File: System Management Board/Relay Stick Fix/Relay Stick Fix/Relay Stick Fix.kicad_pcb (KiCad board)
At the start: 4 copper layers, 28.2 x 27 mm, 17 parts, among them J1 Conn_02x04, Q1 NMOS

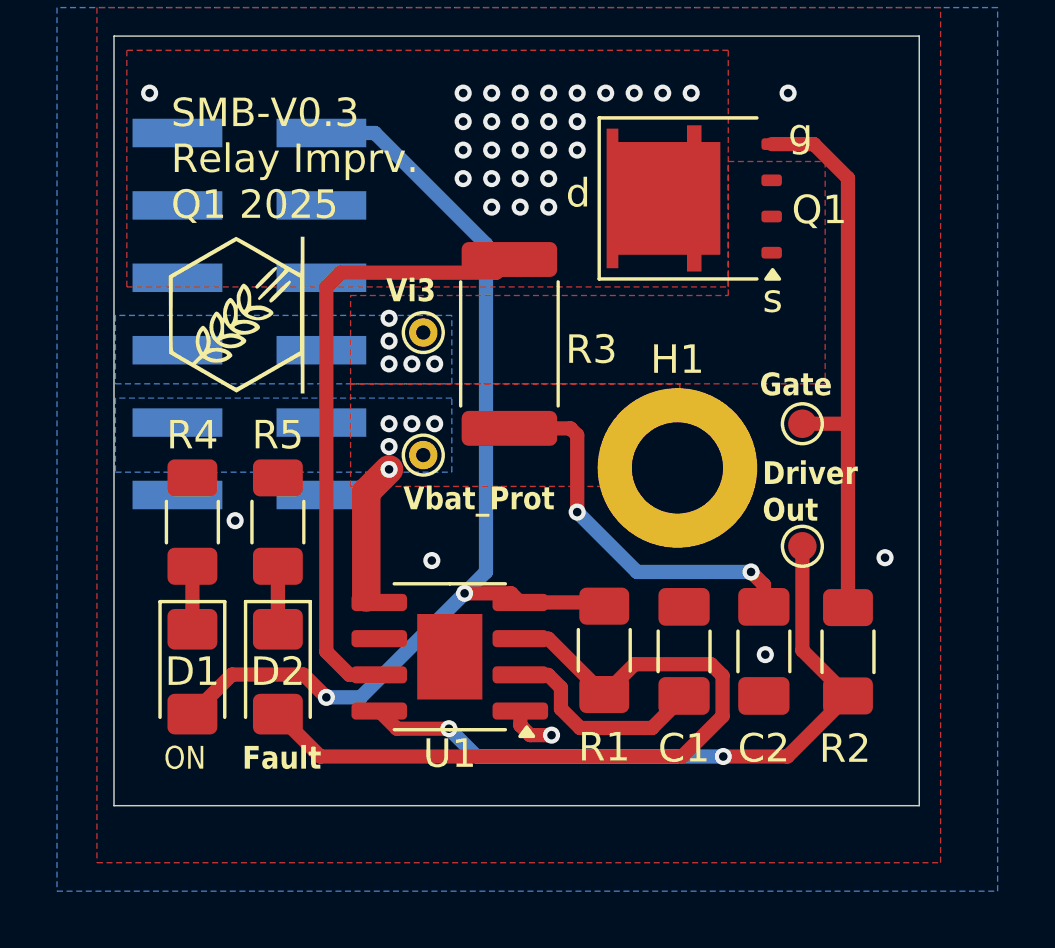
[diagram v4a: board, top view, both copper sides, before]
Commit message: capacitor footprint correction 1210
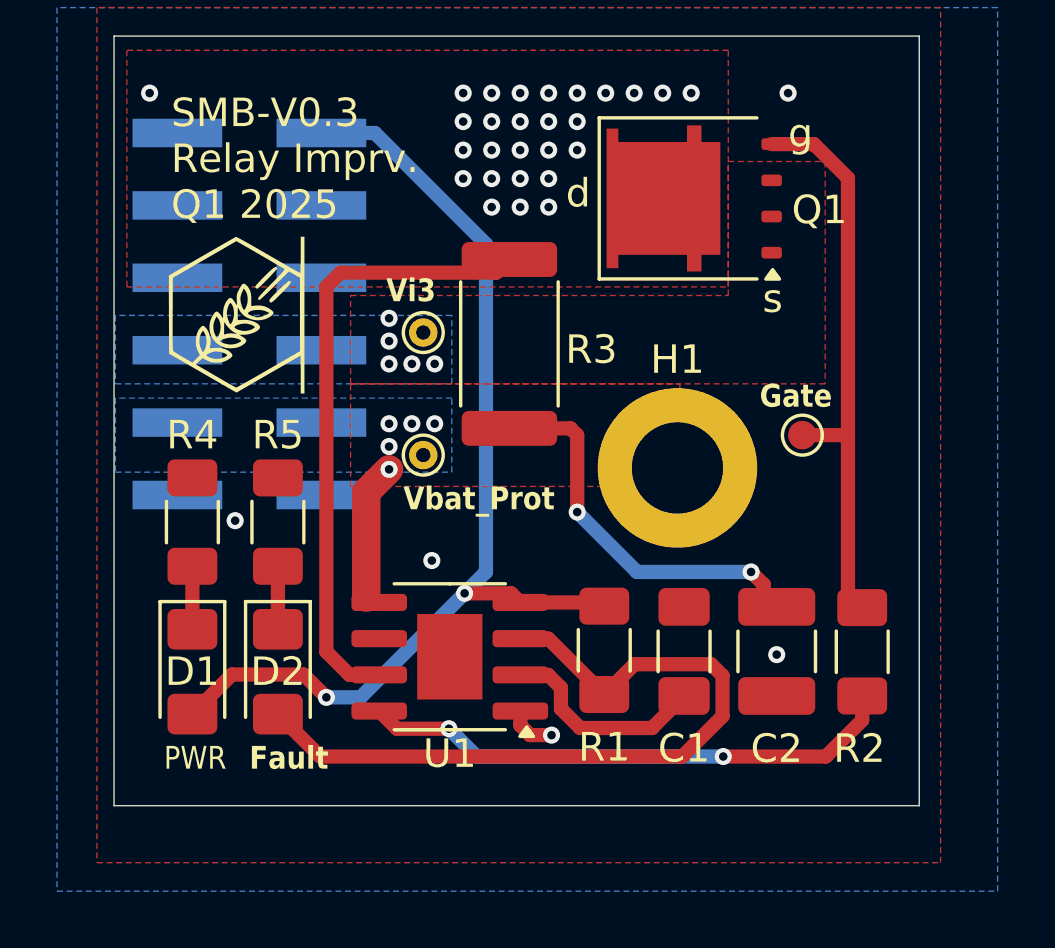
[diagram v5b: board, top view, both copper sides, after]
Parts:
- removed TP1: TestPoint, TestPoint:TestPoint_Pad_D1.0mm
- C2: footprint Capacitor_SMD:C_1206_3216Metric_Pad1.33x1.80mm_HandSolder -> Capacitor_SMD:C_1210_3225Metric_Pad1.33x2.70mm_HandSolder
- J1: value Conn_02x04 -> Conn_02x06
- R4, R5: value 220 -> 280
- moved R2 0.50 mm to (228.0, 138.6)
- moved C2 0.45 mm to (225.0, 138.6)
- moved TP2 0.40 mm to (225.9, 131.0)
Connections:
- net Net-(U1-GATE) renamed /Driver Out
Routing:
- net /Driver Out: track 23.5 -> 19.0 mm
- net GND: vias 7 -> 6
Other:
- board text added: "PWR"
- board text removed: "Driver Out"
- board text removed: "ON"
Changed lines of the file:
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@@
 	(net 6 "/Sense")
 	(net 7 "/Fault")
-	(net 8 "Net-(U1-GATE)")
+	(net 8 "/Driver Out")
 	(net 9 "unconnected-(J1-Pin_3-Pad3)")
 	(net 10 "unconnected-(J1-Pin_4-Pad4)")
@@
 			)
 		)
-		(property "Value" "220"
+		(property "Value" "280"
 			(at 0 1.82 -90)
 			(layer "F.Fab")
@@
 			(layers "F.Cu" "F.Paste" "F.Mask")
 			(roundrect_rratio 0.25)
-			(net 8 "Net-(U1-GATE)")
+			(net 8 "/Driver Out")
 			(pinfunction "GATE")
 			(pintype "input")
@@
 			)
 		)
-		(property "Value" "220"
+		(property "Value" "280"
 			(at 0 1.82 -90)
 			(layer "F.Fab")
@@
 	(footprint "Resistor_SMD:R_1206_3216Metric_Pad1.30x1.75mm_HandSolder"
 		(layer "F.Cu")
-		(at 227.5 138.6 90)
+		(at 228 138.6 90)
 		(descr "Resistor SMD 1206 (3216 Metric), square (rectangular) end terminal, IPC_7351 nominal with elongated pad for handsoldering. (Body size source: IPC-SM-782 page 72, https://www.pcb-3d.com/wordpress/wp-content/uploads/ipc-sm-782a_amendment_1_and_2.pdf), generated with kicad-footprint-generator")
 		(tags "resistor handsolder")
@@
 			(layers "F.Cu" "F.Paste" "F.Mask")
 			(roundrect_rratio 0.192308)
-			(net 8 "Net-(U1-GATE)")
+			(net 8 "/Driver Out")
 			(pintype "passive")
 		)
@@
 		)
 	)
-	(footprint "Capacitor_SMD:C_1206_3216Metric_Pad1.33x1.80mm_HandSolder"
+	(footprint "Capacitor_SMD:C_1210_3225Metric_Pad1.33x2.70mm_HandSolder"
 		(layer "F.Cu")
-		(at 224.55 138.5875 -90)
-		(descr "Capacitor SMD 1206 (3216 Metric), square (rectangular) end terminal, IPC_7351 nominal with elongated pad for handsoldering. (Body size source: IPC-SM-782 page 76, https://www.pcb-3d.com/wordpress/wp-content/uploads/ipc-sm-782a_amendment_1_and_2.pdf), generated with kicad-footprint-generator")
+		(at 225 138.5875 -90)
+		(descr "Capacitor SMD 1210 (3225 Metric), square (rectangular) end terminal, IPC_7351 nominal with elongated pad for handsoldering. (Body size source: IPC-SM-782 page 76, https://www.pcb-3d.com/wordpress/wp-content/uploads/ipc-sm-782a_amendment_1_and_2.pdf), generated with kicad-footprint-generator")
 		(tags "capacitor handsolder")
 		(property "Reference" "C2"
-			(at 3.4 0 180)
+			(at 3.4125 0 0)
 			(layer "F.SilkS")
 			(effects
@@
 		)
 		(property "Value" "10uF"
-			(at 0 1.85 90)
+			(at 0 2.3 -90)
 			(layer "F.Fab")
 			(effects
@@
 			)
 		)
-		(property "Footprint" "Capacitor_SMD:C_1206_3216Metric_Pad1.33x1.80mm_HandSolder"
+		(property "Footprint" "Capacitor_SMD:C_1210_3225Metric_Pad1.33x2.70mm_HandSolder"
 			(at 0 0 -90)
 			(unlocked yes)
@@
 		(attr smd)
 		(fp_line
-			(start -0.711252 0.91)
-			(end 0.711252 0.91)
+			(start -0.711252 1.36)
+			(end 0.711252 1.36)
 			(stroke
 				(width 0.12)
@@
 		)
 		(fp_line
-			(start -0.711252 -0.91)
-			(end 0.711252 -0.91)
+			(start -0.711252 -1.36)
+			(end 0.711252 -1.36)
 			(stroke
 				(width 0.12)
@@
 		)
 		(fp_line
-			(start -2.48 1.15)
-			(end -2.48 -1.15)
+			(start -2.48 1.6)
+			(end -2.48 -1.6)
 			(stroke
 				(width 0.05)
@@
 		)
 		(fp_line
-			(start 2.48 1.15)
-			(end -2.48 1.15)
+			(start 2.48 1.6)
+			(end -2.48 1.6)
 			(stroke
 				(width 0.05)
@@
 		)
 		(fp_line
-			(start -2.48 -1.15)
-			(end 2.48 -1.15)
+			(start -2.48 -1.6)
+			(end 2.48 -1.6)
 			(stroke
 				(width 0.05)
@@
 		)
 		(fp_line
-			(start 2.48 -1.15)
-			(end 2.48 1.15)
+			(start 2.48 -1.6)
+			(end 2.48 1.6)
 			(stroke
 				(width 0.05)
@@
 		)
 		(fp_line
-			(start -1.6 0.8)
-			(end -1.6 -0.8)
+			(start -1.6 1.25)
+			(end -1.6 -1.25)
 			(stroke
 				(width 0.1)
@@
 		)
 		(fp_line
-			(start 1.6 0.8)
-			(end -1.6 0.8)
+			(start 1.6 1.25)
+			(end -1.6 1.25)
 			(stroke
 				(width 0.1)
@@
 		)
 		(fp_line
-			(start -1.6 -0.8)
-			(end 1.6 -0.8)
+			(start -1.6 -1.25)
+			(end 1.6 -1.25)
 			(stroke
 				(width 0.1)
@@
 		)
 		(fp_line
-			(start 1.6 -0.8)
-			(end 1.6 0.8)
+			(start 1.6 -1.25)
+			(end 1.6 1.25)
 			(stroke
 				(width 0.1)
@@
 		)
 		(fp_text user "${REFERENCE}"
-			(at 0 0 90)
+			(at 0 0 -90)
 			(layer "F.Fab")
 			(effects
@@
 		(pad "1" smd roundrect
 			(at -1.5625 0 270)
-			(size 1.325 1.8)
+			(size 1.325 2.7)
 			(layers "F.Cu" "F.Paste" "F.Mask")
 			(roundrect_rratio 0.188679)
@@
 		(pad "2" smd roundrect
 			(at 1.5625 0 270)
-			(size 1.325 1.8)
+			(size 1.325 2.7)
 			(layers "F.Cu" "F.Paste" "F.Mask")
 			(roundrect_rratio 0.188679)
@@
 			(zone_connect 2)
 		)
-		(model "${KICAD8_3DMODEL_DIR}/Capacitor_SMD.3dshapes/C_1206_3216Metric.wrl"
+		(model "${KICAD8_3DMODEL_DIR}/Capacitor_SMD.3dshapes/C_1210_3225Metric.wrl"
 			(offset
 				(xyz 0 0 0)
@@
 	(footprint "TestPoint:TestPoint_Pad_D1.0mm"
 		(layer "F.Cu")
-		(at 225.9 130.6)
+		(at 225.9 131)
 		(descr "SMD pad as test Point, diameter 1.0mm")
 		(tags "test point SMD pad")
@@
 		)
 	)
-	(footprint "TestPoint:TestPoint_Pad_D1.0mm"
-		(layer "F.Cu")
-		(at 225.9 134.9)
-		(descr "SMD pad as test Point, diameter 1.0mm")
-		(tags "test point SMD pad")
-		(property "Reference" "TP1"
-			(at 0 -1.448 0)
-			(layer "F.SilkS")
-			(hide yes)
-			(effects
-				(font
-					(size 1 1)
-					(thickness 0.15)
-				)
-			)
-		)
-		(property "Value" "TestPoint"
-			(at 0 1.55 0)
-			(layer "F.Fab")
-			(effects
-				(font
-					(size 1 1)
-					(thickness 0.15)
-				)
-			)
-		)
-		(property "Footprint" "TestPoint:TestPoint_Pad_D1.0mm"
-			(at 0 0 0)
-			(unlocked yes)
-			(layer "F.Fab")
-			(hide yes)
-			(effects
-				(font
-					(size 1.27 1.27)
-				)
-			)
-		)
-		(property "Datasheet" ""
-			(at 0 0 0)
-			(unlocked yes)
-			(layer "F.Fab")
-			(hide yes)
-			(effects
-				(font
-					(size 1.27 1.27)
-				)
-			)
-		)
-		(property "Description" "test point"
-			(at 0 0 0)
-			(unlocked yes)
-			(layer "F.Fab")
-			(hide yes)
-			(effects
-				(font
-					(size 1.27 1.27)
-				)
-			)
-		)
-		(property ki_fp_filters "Pin* Test*")
-		(sheetname "Root")
-		(sheetfile "Relay Stick Fix.kicad_sch")
-		(attr exclude_from_pos_files)
-		(fp_circle
-			(center 0 0)
-			(end 0 0.7)
-			(stroke
-				(width 0.12)
-				(type solid)
-			)
-			(fill none)
-			(layer "F.SilkS")
-		)
-		(fp_circle
-			(center 0 0)
-			(end 1 0)
-			(stroke
-				(width 0.05)
-				(type solid)
-			)
-			(fill none)
-			(layer "F.CrtYd")
-		)
-		(fp_text user "${REFERENCE}"
-			(at 0 -1.45 0)
-			(layer "F.Fab")
-			(effects
-				(font
-					(size 1 1)
-					(thickness 0.15)
-				)
-			)
-		)
-		(pad "1" smd circle
-			(at 0 0)
-			(size 1 1)
-			(layers "F.Cu" "F.Mask")
-			(net 8 "Net-(U1-GATE)")
-			(pinfunction "1")
-			(pintype "passive")
-		)
-	)
 	(footprint "Connector_PinHeader_2.54mm:PinHeader_2x06_P2.54mm_Vertical_SMD"
 		(layer "B.Cu")
@@
 			)
 		)
-		(property "Value" "Conn_02x04"
+		(property "Value" "Conn_02x06"
 			(at 0 -8.68 180)
 			(layer "B.Fab")
@@
 	)
 	(gr_text "Gate"
-		(at 224.4 129.7 0)
+		(at 224.4 130.1 0)
 		(layer "F.SilkS")
 		(effects
@@
 	)
 	(gr_text "Fault"
-		(at 206.25 142.8 0)
+		(at 206.5 142.8 0)
 		(layer "F.SilkS")
 		(effects
@@
 		)
 	)
-	(gr_text "ON"
+	(gr_text "PWR\n"
 		(at 203.5 142.8 0)
 		(layer "F.SilkS")
@@
 		)
 	)
-	(gr_text "Driver\nOut\n"
-		(at 224.5 134.1 0)
-		(layer "F.SilkS")
-		(effects
-			(font
-				(size 0.8 0.7)
-				(thickness 0.1)
-				(bold yes)
-			)
-			(justify left bottom)
-		)
-	)
 	(gr_text "Vbat_Prot"
 		(at 211.9 133.7 0)
@@
 	)
 	(via
-		(at 228.8 135.3)
-		(size 0.6)
-		(drill 0.3)
-		(layers "F.Cu" "B.Cu")
-		(free yes)
-		(net 1)
-	)
-	(via
 		(at 203 119)
 		(size 0.6)
@@
 	)
 	(via
-		(at 224.6 138.7)
+		(at 225 138.7)
 		(size 0.6)
 		(drill 0.3)
@@
 	)
 	(segment
-		(start 225.375 142.275)
-		(end 227.5 140.15)
-		(width 0.5)
-		(layer "F.Cu")
-		(net 8)
-	)
-	(segment
 		(start 223.125 142.275)
-		(end 225.375 142.275)
+		(end 226.725 142.275)
 		(width 0.5)
 		(layer "F.Cu")
@@
 	)
 	(segment
-		(start 225.9 138.55)
-		(end 225.9 135.3)
+		(start 228 141)
+		(end 228 140.15)
 		(width 0.5)
 		(layer "F.Cu")
@@
 	)
 	(segment
-		(start 227.5 140.15)
-		(end 225.9 138.55)
+		(start 226.725 142.275)
+		(end 228 141)
 		(width 0.5)
 		(layer "F.Cu")
@@
 	)
 	(segment
-		(start 227.5 130.6)
-		(end 225.9 130.6)
+		(start 228 137.05)
+		(end 227.5 136.55)
 		(width 0.5)
 		(layer "F.Cu")
@@
 	)
 	(segment
-		(start 227.5 121.98375)
-		(end 226.30625 120.79)
+		(start 227.5 131)
+		(end 227.5 121.98375)
 		(width 0.5)
 		(layer "F.Cu")
@@
 	)
 	(segment
-		(start 227.5 130.6)
-		(end 227.5 121.98375)
+		(start 227.5 136.55)
+		(end 227.5 131)
 		(width 0.5)
 		(layer "F.Cu")
@@
 	)
 	(segment
-		(start 227.5 137.05)
-		(end 227.5 130.6)
+		(start 226.30625 120.79)
+		(end 224.8225 120.79)
 		(width 0.5)
 		(layer "F.Cu")
@@
 	)
 	(segment
-		(start 226.30625 120.79)
-		(end 224.8225 120.79)
+		(start 227.5 131)
+		(end 225.9 131)
+		(width 0.5)
+		(layer "F.Cu")
+		(net 18)
+	)
+	(segment
+		(start 227.5 121.98375)
+		(end 226.30625 120.79)
 		(width 0.5)
 		(layer "F.Cu")
@@
 	)
 	(group ""
+		(members "bb8eceb2-75df-49de-95a5-31afb5ff107b" "f998aebb-df1a-4666-9337-fedac85aca8c")
+	)
+	(group ""
+		(members "7aa18af9-3efa-4036-90f6-d272eb30f3e6")
+	)
+	(group ""

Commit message: implementing mark's notes
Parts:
- added U2: 74LVC1G04, Package_TO_SOT_SMD:SOT-23-5, F.Cu at (19.9, 37.5)
- C1: value 100nF -> 0.1uF
- R4, R5: value 280 -> 1k
- moved D1 214.7 mm to (18.4, 32.3)
- moved D2 214.7 mm to (21.4, 32.3)
- moved R4 214.7 mm to (18.4, 27.0)
- moved R5 214.7 mm to (21.4, 27.0)
- moved C1 212.0 mm to (35.9, 36.6)
- moved C2 212.0 mm to (39.1, 36.6)
- moved H1 212.0 mm to (35.6, 30.2)
- moved J1 212.0 mm to (20.6, 24.8)
- moved R2 212.0 mm to (42.1, 36.6)
- moved R3 212.0 mm to (29.7, 25.8)
- moved TP2 212.0 mm to (40.0, 29.0)
- moved TP3 212.0 mm to (26.7, 29.7)
- moved TP4 212.0 mm to (26.7, 25.4)
- moved U1 212.0 mm to (27.6, 36.8)
- moved Q1 212.0 mm to (36.2, 20.7)
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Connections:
- D2 pad 2: /Fault -> Net-(D2-A)
- R2 pad 1: /Driver Out -> Net-(U1-GATE)
- U1 pad 5: /Vbat Prot -> Net-(U1-GATE)
- U1 pad 6: unconnected-(U1-NC-Pad6) -> /Sense
- U1 pad 7: /Sense -> unconnected-(U1-NC-Pad7)
- U1 pad 8: /Driver Out -> /Vbat Prot
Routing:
- net Net-(U1-GATE): track 0.00 -> 20.5 mm, vias 0 -> 2
- net /Driver Out: track 19.0 -> 0.00 mm, vias 2 -> 0
- net GND: track 1.74 -> 10.3 mm, vias 6 -> 7
- net /Vbat Prot: track 18.7 -> 24.6 mm, vias 7 -> 9
- net Net-(D2-A): track 0.00 -> 2.80 mm
- net /Fault: track 26.7 -> 29.0 mm
- net /Sense: track 21.8 -> 20.3 mm
- net /5V Bootstrap: track 37.6 -> 38.3 mm

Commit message: zone fix
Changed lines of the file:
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@@
 		(net 1)
 		(net_name "GND")
-		(layers "F.Cu" "In1.Cu")
-		(hatch edge 0.5)
-		(priority 1)
-		(connect_pads
-			(clearance 0.5)
-		)
-		(min_thickness 0.25)
-		(filled_areas_thickness no)
-		(fill yes
-			(thermal_gap 0.5)
-			(thermal_bridge_width 0.5)
-		)
-		(polygon
-			(pts
-				(xy 15.25 14) (xy 15.25 44) (xy 44.85 44) (xy 44.85 14)
-			)
-		)
-	)
-	(zone
-		(net 1)
-		(net_name "GND")
-		(layers "In1.Cu" "B.Cu")
+		(layers "F.Cu" "In1.Cu" "B.Cu")
 		(hatch edge 0.5)
 		(connect_pads
@@
 			)
 		)
+	)
+	(zone
+		(net 6)
+		(net_name "/Sense")
+		(layer "In2.Cu")
+		(hatch edge 0.5)
+		(priority 1)
+		(connect_pads
+			(clearance 0.5)
+		)
+		(min_thickness 0.25)
+		(filled_areas_thickness no)
+		(fill yes
+			(thermal_gap 0.5)
+			(thermal_bridge_width 0.5)
+		)
+		(polygon
+			(pts
+				(xy 15 14.5) (xy 45 14.5) (xy 45 43) (xy 15 43)
+			)
+		)
